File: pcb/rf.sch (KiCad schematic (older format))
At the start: 10 parts, among them U3 STM32W108C8, U4 SE2432L

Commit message: Added more RF stuff and smaller res/cap symbols
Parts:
- removed C10, C8, C9: C, symbol C
- removed R1: 1K5(1%), symbol R
- removed R2, R3: 1K2(1%), symbol R
- added C10, C8, C9: CAP, symbol CAP
- added C11, C13, C? (x5): 100n, symbol CAP
- added C12, C17: 2.2u, symbol CAP
- added C14, C15: 10p, symbol CAP
- added C16, C? (x2): 10n, symbol CAP
- added C?: 1n, symbol CAP
- added R1: 1k8(1%), symbol RES
- added R2: 1k2(1%), symbol RES
- added R3: 180k, symbol RES
- added R4: 1R, symbol RES
- added R?: 10R, symbol RES
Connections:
- net labels added: 1V2, PB6, PB7, PC5, RF_RESET, Vreg
- wire segments 42 -> 149

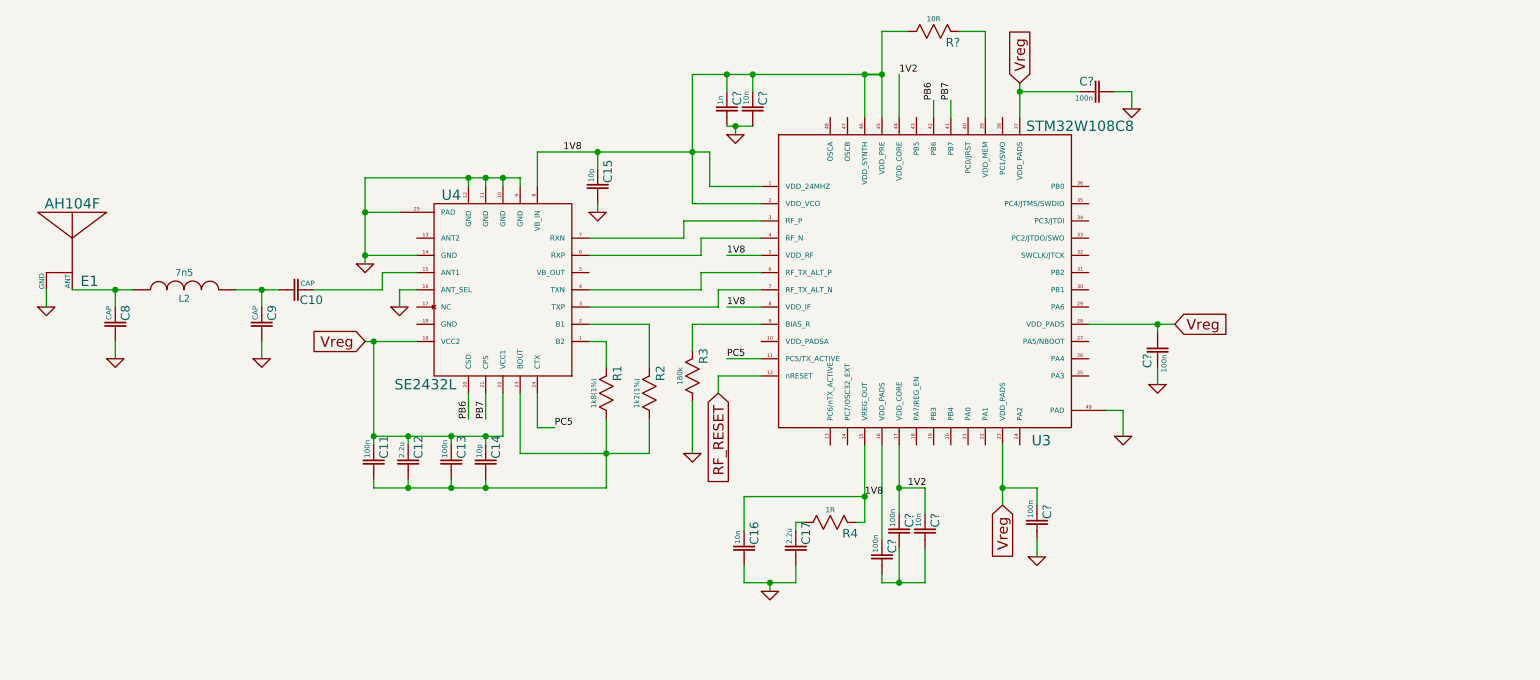
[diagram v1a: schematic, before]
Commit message: Added testpoint component
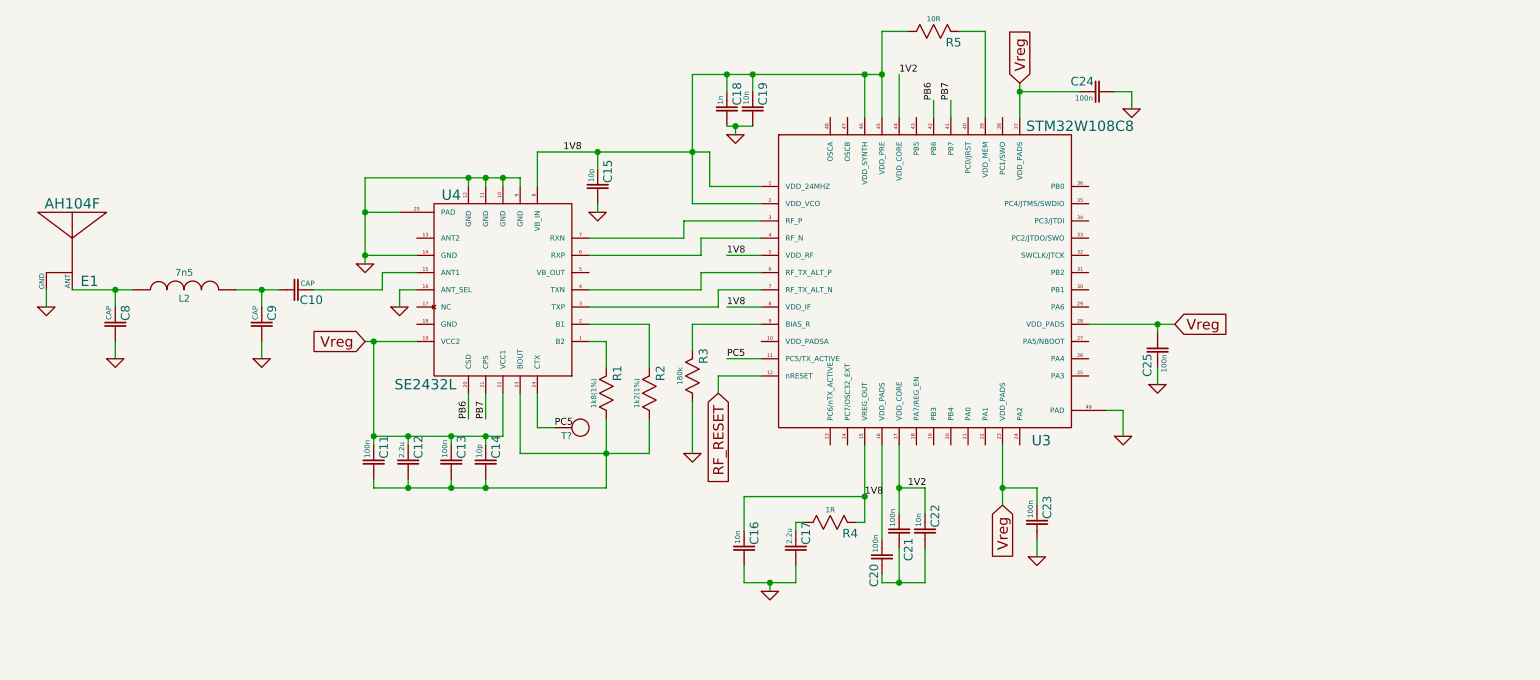
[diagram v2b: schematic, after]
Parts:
- added T?: TP, symbol TP
- gave numbers to parts that had none: 9
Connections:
- net PC5: now also T?.1 (TP)
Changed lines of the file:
@@
-EESchema Schematic File Version 2  date Mon 23 Jul 2012 07:13:55 PM EDT
+EESchema Schematic File Version 2  date Tue 24 Jul 2012 11:45:34 AM EDT
 LIBS:power
 LIBS:device
@@
 LIBS:valves
 LIBS:f4_daughter
+LIBS:f4_daughter-cache
 EELAYER 25  0
 EELAYER END
-$Descr A4 11700 8267
+$Descr A4 11693 8268
 encoding utf-8
 Sheet 2 4
 Title ""
-Date "23 jul 2012"
+Date "24 jul 2012"
 Rev ""
 Comp ""
@@
 Connection ~ 8250 4300
 Wire Wire Line
-	8350 4300 8250 4300
-Wire Wire Line
-	8250 4300 7850 4300
+	7850 4300 8250 4300
+Wire Wire Line
+	8250 4300 8350 4300
 Connection ~ 6650 2850
 Wire Wire Line
-	6650 2850 6650 2600
+	6650 2600 6650 2850
+Wire Wire Line
+	6650 2850 6650 3100
 Wire Wire Line
 	6650 2600 6800 2600
@@
 Connection ~ 5550 3300
 Wire Wire Line
-	5650 3300 5550 3300
-Wire Wire Line
-	5550 3300 5000 3300
-Wire Wire Line
-	5000 3300 4650 3300
+	4650 3300 5000 3300
+Wire Wire Line
+	5000 3300 5550 3300
+Wire Wire Line
+	5550 3300 5650 3300
 Wire Wire Line
 	5650 3300 5650 3500
@@
 	5000 3650 5000 3600
 Wire Wire Line
-	6500 5450 6550 5450
-Wire Wire Line
-	6550 5450 6550 5300
-Wire Wire Line
-	6550 5300 6550 5000
-Wire Wire Line
-	5300 4850 5300 5050
+	6550 5450 6500 5450
+Wire Wire Line
+	6550 5000 6550 5300
+Wire Wire Line
+	6550 5300 6550 5450
+Wire Wire Line
+	5300 5050 5300 4850
 Wire Wire Line
 	5050 4550 5050 4400
 Connection ~ 5050 5050
 Wire Wire Line
-	5300 5050 5050 5050
-Wire Wire Line
-	5050 5050 4550 5050
+	4550 5050 5050 5050
+Wire Wire Line
+	5050 5050 5300 5050
 Wire Wire Line
 	4950 4300 5300 4300
@@
 Connection ~ 4450 3450
 Wire Wire Line
-	4550 3500 4550 3450
+	4550 3450 4550 3500
 Wire Wire Line
 	4350 3450 4350 3500
@@
 Connection ~ 4350 3450
 Wire Wire Line
-	4550 3450 4450 3450
-Wire Wire Line
-	4450 3450 4350 3450
-Wire Wire Line
-	4350 3450 4250 3450
-Wire Wire Line
-	4250 3450 3650 3450
+	3650 3450 4250 3450
+Wire Wire Line
+	4250 3450 4350 3450
+Wire Wire Line
+	4350 3450 4450 3450
+Wire Wire Line
+	4450 3450 4550 3450
 Wire Wire Line
 	3650 3450 3650 3650
@@
 	3750 4100 3350 4100
 Wire Wire Line
-	6150 5700 6150 5800
-Wire Wire Line
-	6150 5800 6000 5800
-Wire Wire Line
-	6000 5800 5850 5800
+	6150 5800 6150 5700
+Wire Wire Line
+	5850 5800 6000 5800
+Wire Wire Line
+	6000 5800 6150 5800
 Wire Wire Line
 	5850 5800 5850 5700
@@
 Connection ~ 3900 5250
 Wire Wire Line
-	3700 5250 3900 5250
-Wire Wire Line
-	3900 5250 4150 5250
-Wire Wire Line
-	4150 5250 4350 5250
-Wire Wire Line
-	4350 5250 5050 5250
-Wire Wire Line
-	5050 5250 5050 5050
-Wire Wire Line
-	5050 5050 5050 4850
+	5050 5250 4350 5250
+Wire Wire Line
+	4350 5250 4150 5250
+Wire Wire Line
+	4150 5250 3900 5250
+Wire Wire Line
+	3900 5250 3700 5250
+Wire Wire Line
+	5050 4850 5050 5050
+Wire Wire Line
+	5050 5050 5050 5250
 Connection ~ 4350 5250
 Wire Wire Line
@@
 	6900 5800 6900 5600
 Wire Wire Line
-	5950 3600 5550 3600
+	5550 3600 5950 3600
 Connection ~ 5000 3300
 Wire Wire Line
 	5800 3200 5800 3150
 Wire Wire Line
-	5550 3600 5550 3300
-Wire Wire Line
-	5550 3300 5550 2850
+	5550 2850 5550 3300
+Wire Wire Line
+	5550 3300 5550 3600
 Wire Wire Line
 	5550 2850 5750 2850
@@
 	5750 2850 5900 2850
 Wire Wire Line
-	5900 2850 6650 2850
-Wire Wire Line
-	6650 2850 6550 2850
+	5900 2850 6550 2850
 Wire Wire Line
 	6550 2850 6650 2850
-Wire Wire Line
-	6650 2850 6650 3100
 Wire Wire Line
 	6750 3100 6750 2850
@@
 PC5
 $Comp
-L GND #PWR?
+L GND #PWR13
 U 1 1 500DD937
 P 8250 4650
-F 0 "#PWR?" H 8250 4650 30  0001 C CNN
+F 0 "#PWR13" H 8250 4650 30  0001 C CNN
 F 1 "GND" H 8250 4580 30  0001 C CNN
 	1    8250 4650
@@
 $EndComp
 $Comp
-L CAP C?
+L CAP C25
 U 1 1 500DD930
 P 8250 4450
-F 0 "C?" H 8270 4420 50  0000 L TNN
+F 0 "C25" H 8270 4420 50  0000 L TNN
 F 1 "100n" H 8275 4470 30  0000 L BNN
 	1    8250 4450
@@
 Vreg
 $Comp
-L RES R?
+L RES R5
 U 1 1 500DD912
 P 6950 2600
-F 0 "R?" H 7020 2565 50  0000 L TNN
+F 0 "R5" H 7020 2565 50  0000 L TNN
 F 1 "10R" H 6950 2655 30  0000 C BNN
 	1    6950 2600
@@
 $EndComp
 $Comp
-L GND #PWR?
+L GND #PWR5
 U 1 1 500DD8E1
 P 3850 4200
-F 0 "#PWR?" H 3850 4200 30  0001 C CNN
+F 0 "#PWR5" H 3850 4200 30  0001 C CNN
 F 1 "GND" H 3850 4130 30  0001 C CNN
 	1    3850 4200
@@
 $EndComp
 $Comp
-L GND #PWR?
+L GND #PWR12
 U 1 1 500DD883
 P 8100 3050
-F 0 "#PWR?" H 8100 3050 30  0001 C CNN
+F 0 "#PWR12" H 8100 3050 30  0001 C CNN
 F 1 "GND" H 8100 2980 30  0001 C CNN
 	1    8100 3050
@@
 $EndComp
 $Comp
-L CAP C?
+L CAP C24
 U 1 1 500DD879
 P 7900 2950
-F 0 "C?" H 7920 2920 50  0000 L TNN
+F 0 "C24" H 7920 2920 50  0000 L TNN
 F 1 "100n" H 7925 2970 30  0000 L BNN
 	1    7900 2950
@@
 1V2
 $Comp
-L GND #PWR?
+L GND #PWR8
 U 1 1 500DD7C0
 P 5800 3200
-F 0 "#PWR?" H 5800 3200 30  0001 C CNN
+F 0 "#PWR8" H 5800 3200 30  0001 C CNN
 F 1 "GND" H 5800 3130 30  0001 C CNN
 	1    5800 3200
@@
 $EndComp
 $Comp
-L CAP C?
+L CAP C19
 U 1 1 500DD7BD
 P 5900 3050
-F 0 "C?" H 5920 3020 50  0000 L TNN
+F 0 "C19" H 5920 3020 50  0000 L TNN
 F 1 "10n" H 5925 3070 30  0000 L BNN
 	1    5900 3050
@@
 $EndComp
 $Comp
-L CAP C?
+L CAP C18
 U 1 1 500DD7BB
 P 5750 3050
-F 0 "C?" H 5770 3020 50  0000 L TNN
+F 0 "C18" H 5770 3020 50  0000 L TNN
 F 1 "1n" H 5775 3070 30  0000 L BNN
 	1    5750 3050
@@
 1V8
 $Comp
-L CAP C?
+L CAP C20
 U 1 1 500DD74C
 P 6650 5650
-F 0 "C?" H 6670 5620 50  0000 L TNN
+F 0 "C20" H 6475 5725 50  0000 L TNN
 F 1 "100n" H 6675 5670 30  0000 L BNN
 	1    6650 5650
@@
 $EndComp
 $Comp
-L CAP C?
+L CAP C22
 U 1 1 500DD703
 P 6900 5500
-F 0 "C?" H 6920 5470 50  0000 L TNN
+F 0 "C22" H 6920 5470 50  0000 L TNN
 F 1 "10n" H 6925 5520 30  0000 L BNN
 	1    6900 5500
@@
 $EndComp
 $Comp
-L CAP C?
+L CAP C21
 U 1 1 500DD700
 P 6750 5500
-F 0 "C?" H 6770 5470 50  0000 L TNN
+F 0 "C21" H 6575 5475 50  0000 L TNN
 F 1 "100n" H 6775 5520 30  0000 L BNN
 	1    6750 5500
@@
 $EndComp
 $Comp
-L GND #PWR?
+L GND #PWR10
 U 1 1 500DD6F0
 P 7550 5650
-F 0 "#PWR?" H 7550 5650 30  0001 C CNN
+F 0 "#PWR10" H 7550 5650 30  0001 C CNN
 F 1 "GND" H 7550 5580 30  0001 C CNN
 	1    7550 5650
@@
 $EndComp
 $Comp
-L CAP C?
+L CAP C23
 U 1 1 500DD6E3
 P 7550 5450
-F 0 "C?" H 7570 5420 50  0000 L TNN
+F 0 "C23" H 7570 5420 50  0000 L TNN
 F 1 "100n" H 7575 5470 30  0000 L BNN
 	1    7550 5450
@@
 Vreg
 $Comp
-L GND #PWR5
+L GND #PWR6
 U 1 1 500DD2FF
 P 5000 3650
-F 0 "#PWR5" H 5000 3650 30  0001 C CNN
+F 0 "#PWR6" H 5000 3650 30  0001 C CNN
 F 1 "GND" H 5000 3580 30  0001 C CNN
 	1    5000 3650
@@
 $EndComp
 $Comp
-L GND #PWR7
+L GND #PWR9
 U 1 1 500DD1EA
 P 6000 5850
-F 0 "#PWR7" H 6000 5850 30  0001 C CNN
+F 0 "#PWR9" H 6000 5850 30  0001 C CNN
 F 1 "GND" H 6000 5780 30  0001 C CNN
 	1    6000 5850
@@
 $EndComp
 $Comp
-L GND #PWR6
+L GND #PWR7
 U 1 1 500DCCCC
 P 5550 5050
-F 0 "#PWR6" H 5550 5050 30  0001 C CNN
+F 0 "#PWR7" H 5550 5050 30  0001 C CNN
 F 1 "GND" H 5550 4980 30  0001 C CNN
 	1    5550 5050
@@
 $EndComp
 $Comp
-L GND #PWR8
+L GND #PWR11
 U 1 1 500DCA3C
 P 8050 4950
-F 0 "#PWR8" H 8050 4950 30  0001 C CNN
+F 0 "#PWR11" H 8050 4950 30  0001 C CNN
 F 1 "GND" H 8050 4880 30  0001 C CNN
 	1    8050 4950
@@
 	1    0    0    -1
 $EndComp
+$Comp
+L TP T?
+U 1 1 500EC307
+P 4850 4900
+F 0 "T?" H 4850 4875 40  0000 R TNN
+F 1 "TP" H 4800 4950 60  0001 C CNN
+	1    4850 4900
+	1    0    0    -1
+$EndComp

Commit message: Added FT230X
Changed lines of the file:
@@
-EESchema Schematic File Version 2  date Tue 24 Jul 2012 11:45:34 AM EDT
+EESchema Schematic File Version 2  date Wed 25 Jul 2012 06:59:20 PM EDT
 LIBS:power
 LIBS:device
@@
 EELAYER 25  0
 EELAYER END
-$Descr A4 11693 8268
+$Descr A4 11700 8267
 encoding utf-8
 Sheet 2 4
 Title ""
-Date "24 jul 2012"
+Date "25 jul 2012"
 Rev ""
 Comp ""
@@
 Connection ~ 8250 4300
 Wire Wire Line
-	7850 4300 8250 4300
-Wire Wire Line
-	8250 4300 8350 4300
+	7850 4300 8350 4300
 Connection ~ 6650 2850
 Wire Wire Line
-	6650 2600 6650 2850
-Wire Wire Line
-	6650 2850 6650 3100
+	6650 3100 6650 2600
 Wire Wire Line
 	6650 2600 6800 2600
@@
 Connection ~ 5800 3150
 Wire Wire Line
-	5750 3150 5800 3150
-Wire Wire Line
-	5800 3150 5900 3150
+	5750 3150 5900 3150
 Connection ~ 5550 3300
 Wire Wire Line
-	4650 3300 5000 3300
-Wire Wire Line
-	5000 3300 5550 3300
-Wire Wire Line
-	5550 3300 5650 3300
+	5650 3300 4650 3300
 Wire Wire Line
 	5650 3300 5650 3500
@@
 	5650 3500 5950 3500
 Wire Wire Line
-	6650 5750 6650 5800
+	6650 5800 6650 5750
 Wire Wire Line
 	6750 5600 6750 5800
@@
 Connection ~ 6750 5250
 Wire Wire Line
-	6750 5250 6900 5250
+	6900 5250 6750 5250
 Wire Wire Line
 	6900 5250 6900 5400
 Connection ~ 7350 5250
 Wire Wire Line
-	7350 5250 7550 5250
+	7550 5250 7350 5250
 Wire Wire Line
 	7550 5250 7550 5350
@@
 Connection ~ 4150 5250
 Wire Wire Line
-	4350 5250 4350 5200
-Wire Wire Line
-	3900 5200 3900 5250
-Wire Wire Line
-	3700 5200 3700 5250
+	4350 5200 4350 5250
+Wire Wire Line
+	3900 5250 3900 5200
+Wire Wire Line
+	3700 5250 3700 5200
 Connection ~ 4150 4950
 Wire Wire Line
@@
 Connection ~ 3700 4950
 Wire Wire Line
-	3700 4400 3700 4950
-Wire Wire Line
-	3700 4950 3700 5000
-Wire Wire Line
-	3650 4400 3700 4400
-Wire Wire Line
-	3700 4400 3950 4400
+	3700 5000 3700 4400
+Wire Wire Line
+	3650 4400 3950 4400
 Connection ~ 6550 5300
 Wire Wire Line
-	6550 5300 5850 5300
+	5850 5300 6550 5300
 Wire Wire Line
 	5850 5300 5850 5500
@@
 	6550 5450 6500 5450
 Wire Wire Line
-	6550 5000 6550 5300
-Wire Wire Line
-	6550 5300 6550 5450
+	6550 5000 6550 5450
 Wire Wire Line
 	5300 5050 5300 4850
@@
 Connection ~ 5050 5050
 Wire Wire Line
-	4550 5050 5050 5050
-Wire Wire Line
-	5050 5050 5300 5050
+	5300 5050 4550 5050
 Wire Wire Line
 	4950 4300 5300 4300
@@
 	4350 3450 4350 3500
 Wire Wire Line
-	4250 3450 4250 3500
+	4250 3500 4250 3450
 Wire Wire Line
 	3650 3900 3950 3900
@@
 Connection ~ 2200 4100
 Wire Wire Line
-	1950 4100 2200 4100
-Wire Wire Line
-	2200 4100 2300 4100
+	1950 4100 2300 4100
 Wire Wire Line
 	1800 4200 1800 4100
 Wire Wire Line
-	2900 4100 3050 4100
-Wire Wire Line
-	3050 4100 3150 4100
+	2900 4100 3150 4100
 Connection ~ 3050 4100
 Wire Wire Line
@@
 Connection ~ 3650 3900
 Wire Wire Line
-	4450 3500 4450 3450
+	4450 3450 4450 3500
 Connection ~ 4350 3450
 Wire Wire Line
-	3650 3450 4250 3450
-Wire Wire Line
-	4250 3450 4350 3450
-Wire Wire Line
-	4350 3450 4450 3450
-Wire Wire Line
-	4450 3450 4550 3450
-Wire Wire Line
-	3650 3450 3650 3650
-Wire Wire Line
-	3650 3650 3650 3900
-Wire Wire Line
-	3650 3900 3650 3950
+	3650 3450 4550 3450
+Wire Wire Line
+	3650 3950 3650 3450
 Connection ~ 3650 3650
 Connection ~ 4250 3450
@@
 	6150 5800 6150 5700
 Wire Wire Line
-	5850 5800 6000 5800
-Wire Wire Line
-	6000 5800 6150 5800
+	6150 5800 5850 5800
 Wire Wire Line
 	5850 5800 5850 5700
@@
 Connection ~ 3700 4400
 Wire Wire Line
-	3700 4950 3900 4950
-Wire Wire Line
-	3900 4950 4150 4950
-Wire Wire Line
-	4150 4950 4350 4950
-Wire Wire Line
-	4350 4950 4450 4950
+	3700 4950 4450 4950
 Wire Wire Line
 	4450 4950 4450 4700
@@
 Connection ~ 3900 5250
 Wire Wire Line
-	5050 5250 4350 5250
-Wire Wire Line
-	4350 5250 4150 5250
-Wire Wire Line
-	4150 5250 3900 5250
-Wire Wire Line
-	3900 5250 3700 5250
-Wire Wire Line
-	5050 4850 5050 5050
-Wire Wire Line
-	5050 5050 5050 5250
+	5050 5250 3700 5250
+Wire Wire Line
+	5050 4850 5050 5250
 Connection ~ 4350 5250
 Wire Wire Line
-	7350 5000 7350 5250
-Wire Wire Line
-	7350 5250 7350 5350
+	7350 5000 7350 5350
 Wire Wire Line
 	7550 5650 7550 5550
 Wire Wire Line
-	6750 5000 6750 5250
-Wire Wire Line
-	6750 5250 6750 5400
-Wire Wire Line
-	6650 5800 6750 5800
-Wire Wire Line
-	6750 5800 6900 5800
+	6750 5000 6750 5400
+Wire Wire Line
+	6650 5800 6900 5800
 Wire Wire Line
 	6900 5800 6900 5600
@@
 	5800 3200 5800 3150
 Wire Wire Line
-	5550 2850 5550 3300
-Wire Wire Line
-	5550 3300 5550 3600
-Wire Wire Line
-	5550 2850 5750 2850
-Wire Wire Line
-	5750 2850 5900 2850
-Wire Wire Line
-	5900 2850 6550 2850
-Wire Wire Line
-	6550 2850 6650 2850
+	5550 2850 5550 3600
+Wire Wire Line
+	6650 2850 5550 2850
 Wire Wire Line
 	6750 3100 6750 2850
@@
 	8100 2950 8000 2950
 Wire Wire Line
-	7450 2900 7450 2950
-Wire Wire Line
-	7450 2950 7450 3100
+	7450 2900 7450 3100
 Connection ~ 7450 2950
 Wire Wire Line
@@
 PC5
 $Comp
-L GND #PWR13
+L GND #PWR01
 U 1 1 500DD937
 P 8250 4650
-F 0 "#PWR13" H 8250 4650 30  0001 C CNN
+F 0 "#PWR01" H 8250 4650 30  0001 C CNN
 F 1 "GND" H 8250 4580 30  0001 C CNN
 	1    8250 4650
@@
 $EndComp
 $Comp
-L GND #PWR5
+L GND #PWR02
 U 1 1 500DD8E1
 P 3850 4200
-F 0 "#PWR5" H 3850 4200 30  0001 C CNN
+F 0 "#PWR02" H 3850 4200 30  0001 C CNN
 F 1 "GND" H 3850 4130 30  0001 C CNN
 	1    3850 4200
@@
 $EndComp
 $Comp
-L GND #PWR12
+L GND #PWR03
 U 1 1 500DD883
 P 8100 3050
-F 0 "#PWR12" H 8100 3050 30  0001 C CNN
+F 0 "#PWR03" H 8100 3050 30  0001 C CNN
 F 1 "GND" H 8100 2980 30  0001 C CNN
 	1    8100 3050
@@
 1V2
 $Comp
-L GND #PWR8
+L GND #PWR04
 U 1 1 500DD7C0
 P 5800 3200
-F 0 "#PWR8" H 5800 3200 30  0001 C CNN
+F 0 "#PWR04" H 5800 3200 30  0001 C CNN
 F 1 "GND" H 5800 3130 30  0001 C CNN
 	1    5800 3200
@@
 $EndComp
 $Comp
-L GND #PWR10
+L GND #PWR05
 U 1 1 500DD6F0
 P 7550 5650
-F 0 "#PWR10" H 7550 5650 30  0001 C CNN
+F 0 "#PWR05" H 7550 5650 30  0001 C CNN
 F 1 "GND" H 7550 5580 30  0001 C CNN
 	1    7550 5650
@@
 Vreg
 $Comp
-L GND #PWR6
+L GND #PWR06
 U 1 1 500DD2FF
 P 5000 3650
-F 0 "#PWR6" H 5000 3650 30  0001 C CNN
+F 0 "#PWR06" H 5000 3650 30  0001 C CNN
 F 1 "GND" H 5000 3580 30  0001 C CNN
 	1    5000 3650
@@
 $EndComp
 $Comp
-L GND #PWR9
+L GND #PWR07
 U 1 1 500DD1EA
 P 6000 5850
-F 0 "#PWR9" H 6000 5850 30  0001 C CNN
+F 0 "#PWR07" H 6000 5850 30  0001 C CNN
 F 1 "GND" H 6000 5780 30  0001 C CNN
 	1    6000 5850
@@
 $EndComp
 $Comp
-L GND #PWR7
+L GND #PWR08
 U 1 1 500DCCCC
 P 5550 5050
-F 0 "#PWR7" H 5550 5050 30  0001 C CNN
+F 0 "#PWR08" H 5550 5050 30  0001 C CNN
 F 1 "GND" H 5550 4980 30  0001 C CNN
 	1    5550 5050
@@
 1V8
 $Comp
-L GND #PWR3
+L GND #PWR09
 U 1 1 500DCAB4
 P 3050 4500
-F 0 "#PWR3" H 3050 4500 30  0001 C CNN
+F 0 "#PWR09" H 3050 4500 30  0001 C CNN
 F 1 "GND" H 3050 4430 30  0001 C CNN
 	1    3050 4500
@@
 $EndComp
 $Comp
-L GND #PWR2
+L GND #PWR010
 U 1 1 500DCAB1
 P 2200 4500
-F 0 "#PWR2" H 2200 4500 30  0001 C CNN
+F 0 "#PWR010" H 2200 4500 30  0001 C CNN
 F 1 "GND" H 2200 4430 30  0001 C CNN
 	1    2200 4500
@@
 $EndComp
 $Comp
-L GND #PWR4
+L GND #PWR011
 U 1 1 500DCAA7
 P 3650 3950
-F 0 "#PWR4" H 3650 3950 30  0001 C CNN
+F 0 "#PWR011" H 3650 3950 30  0001 C CNN
 F 1 "GND" H 3650 3880 30  0001 C CNN
 	1    3650 3950
@@
 $EndComp
 $Comp
-L GND #PWR1
+L GND #PWR012
 U 1 1 500DCA40
 P 1800 4200
-F 0 "#PWR1" H 1800 4200 30  0001 C CNN
+F 0 "#PWR012" H 1800 4200 30  0001 C CNN
 F 1 "GND" H 1800 4130 30  0001 C CNN
 	1    1800 4200
@@
 $EndComp
 $Comp
-L GND #PWR11
+L GND #PWR013
 U 1 1 500DCA3C
 P 8050 4950
-F 0 "#PWR11" H 8050 4950 30  0001 C CNN
+F 0 "#PWR013" H 8050 4950 30  0001 C CNN
 F 1 "GND" H 8050 4880 30  0001 C CNN
 	1    8050 4950
